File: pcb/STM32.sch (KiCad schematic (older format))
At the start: 43 parts

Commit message: stepper planes
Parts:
- removed RA1, RA2, RA3, RA4, RA5, RA6, RA7, RA8, RA9: 100k, Resistors_SMD:R_0603, symbol media_board:R-RESCUE-stamp_mini_4_layers
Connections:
- wire segments 209 -> 182
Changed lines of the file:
@@
 IO32
-$Comp
-L media_board:R-RESCUE-stamp_mini_4_layers RA1
-U 1 1 55660488
-P 850 2800
-F 0 "RA1" V 930 2800 50  0000 C CNN
-F 1 "100k" V 850 2800 50  0000 C CNN
-F 2 "Resistors_SMD:R_0603" H 850 2800 60  0001 C CNN
-F 3 "" H 850 2800 60  0001 C CNN
-	1    850  2800
-	-1   0    0    1
-$EndComp
-$Comp
-L media_board:R-RESCUE-stamp_mini_4_layers RA2
-U 1 1 55660A61
-P 1000 2800
-F 0 "RA2" V 1080 2800 50  0000 C CNN
-F 1 "100k" V 1000 2800 50  0000 C CNN
-F 2 "Resistors_SMD:R_0603" H 1000 2800 60  0001 C CNN
-F 3 "" H 1000 2800 60  0001 C CNN
-	1    1000 2800
-	-1   0    0    1
-$EndComp
-$Comp
-L media_board:R-RESCUE-stamp_mini_4_layers RA3
-U 1 1 55660AB1
-P 1150 2800
-F 0 "RA3" V 1230 2800 50  0000 C CNN
-F 1 "100k" V 1150 2800 50  0000 C CNN
-F 2 "Resistors_SMD:R_0603" H 1150 2800 60  0001 C CNN
-F 3 "" H 1150 2800 60  0001 C CNN
-	1    1150 2800
-	-1   0    0    1
-$EndComp
-$Comp
-L media_board:R-RESCUE-stamp_mini_4_layers RA4
-U 1 1 55660AFE
-P 1300 2800
-F 0 "RA4" V 1380 2800 50  0000 C CNN
-F 1 "100k" V 1300 2800 50  0000 C CNN
-F 2 "Resistors_SMD:R_0603" H 1300 2800 60  0001 C CNN
-F 3 "" H 1300 2800 60  0001 C CNN
-	1    1300 2800
-	-1   0    0    1
-$EndComp
-$Comp
-L media_board:R-RESCUE-stamp_mini_4_layers RA5
-U 1 1 55660B50
-P 1450 2800
-F 0 "RA5" V 1530 2800 50  0000 C CNN
-F 1 "100k" V 1450 2800 50  0000 C CNN
-F 2 "Resistors_SMD:R_0603" H 1450 2800 60  0001 C CNN
-F 3 "" H 1450 2800 60  0001 C CNN
-	1    1450 2800
-	-1   0    0    1
-$EndComp
-$Comp
-L media_board:R-RESCUE-stamp_mini_4_layers RA6
-U 1 1 55660BA7
-P 1600 2800
-F 0 "RA6" V 1680 2800 50  0000 C CNN
-F 1 "100k" V 1600 2800 50  0000 C CNN
-F 2 "Resistors_SMD:R_0603" H 1600 2800 60  0001 C CNN
-F 3 "" H 1600 2800 60  0001 C CNN
-	1    1600 2800
-	-1   0    0    1
-$EndComp
-$Comp
-L media_board:R-RESCUE-stamp_mini_4_layers RA7
-U 1 1 55660C05
-P 1750 2800
-F 0 "RA7" V 1830 2800 50  0000 C CNN
-F 1 "100k" V 1750 2800 50  0000 C CNN
-F 2 "Resistors_SMD:R_0603" H 1750 2800 60  0001 C CNN
-F 3 "" H 1750 2800 60  0001 C CNN
-	1    1750 2800
-	-1   0    0    1
-$EndComp
-$Comp
-L media_board:R-RESCUE-stamp_mini_4_layers RA8
-U 1 1 55660C68
-P 1900 2800
-F 0 "RA8" V 1980 2800 50  0000 C CNN
-F 1 "100k" V 1900 2800 50  0000 C CNN
-F 2 "Resistors_SMD:R_0603" H 1900 2800 60  0001 C CNN
-F 3 "" H 1900 2800 60  0001 C CNN
-	1    1900 2800
-	-1   0    0    1
-$EndComp
-$Comp
-L media_board:GND-RESCUE-stamp_mini_4_layers #PWR0168
-U 1 1 556636B2
-P 850 3150
-F 0 "#PWR0168" H 850 3150 30  0001 C CNN
-F 1 "GND" H 850 3080 30  0001 C CNN
-F 2 "" H 850 3150 60  0001 C CNN
-F 3 "" H 850 3150 60  0001 C CNN
-	1    850  3150
-	1    0    0    -1
-$EndComp
 $Comp
 L media_board:JUMPER PGM1
@@
 	5050 6650 5050 6750
 Wire Wire Line
-	750  1800 1900 1800
-Wire Wire Line
 	2250 3900 2600 3900
 Wire Wire Line
@@
 	2600 3300 2250 3300
 Wire Wire Line
-	750  2500 850  2500
-Wire Wire Line
-	750  2300 1150 2300
-Wire Wire Line
-	750  2100 1450 2100
-Wire Wire Line
-	750  1900 1750 1900
-Wire Wire Line
 	4250 6550 4250 6650
 Wire Wire Line
@@
 	2300 1400 2600 1400
 Wire Wire Line
-	750  2000 1600 2000
-Wire Wire Line
 	4500 800  4500 950
 Wire Wire Line
@@
 Wire Wire Line
 	2250 3800 2600 3800
-Wire Wire Line
-	750  2200 1300 2200
-Wire Wire Line
-	750  2400 1000 2400
 Wire Wire Line
 	4250 6650 4450 6650
@@
 Wire Wire Line
 	6000 4200 5600 4200
-Wire Wire Line
-	850  2550 850  2500
-Connection ~ 850  2500
-Wire Wire Line
-	1000 2550 1000 2400
-Connection ~ 1000 2400
-Wire Wire Line
-	1150 2550 1150 2300
-Connection ~ 1150 2300
-Wire Wire Line
-	1300 2550 1300 2200
-Connection ~ 1300 2200
-Wire Wire Line
-	1450 2550 1450 2100
-Connection ~ 1450 2100
-Wire Wire Line
-	1600 2550 1600 2000
-Connection ~ 1600 2000
-Wire Wire Line
-	1750 2550 1750 1900
-Connection ~ 1750 1900
-Wire Wire Line
-	1900 2550 1900 1800
-Connection ~ 1900 1800
-Wire Wire Line
-	850  3050 850  3150
 Wire Wire Line
 	7400 7900 7550 7900
@@
 Wire Wire Line
 	6900 3550 7200 3550
-Wire Wire Line
-	850  2500 2600 2500
-Wire Wire Line
-	1000 2400 2600 2400
-Wire Wire Line
-	1150 2300 2600 2300
-Wire Wire Line
-	1300 2200 2600 2200
-Wire Wire Line
-	1450 2100 2600 2100
-Wire Wire Line
-	1600 2000 2600 2000
-Wire Wire Line
-	1750 1900 2600 1900
-Wire Wire Line
-	1900 1800 2600 1800
 Wire Wire Line
 	5600 1950 6900 1950
@@
 Text Label 800  3500 0    50   ~ 0
 SEN8
-Wire Wire Line
-	750  3500 850  3500
-Wire Wire Line
-	850  3550 850  3500
-Connection ~ 850  3500
-Wire Wire Line
-	850  3500 2600 3500
-$Comp
-L media_board:R-RESCUE-stamp_mini_4_layers RA9
-U 1 1 5EA6155C
-P 850 3800
-F 0 "RA9" V 930 3800 50  0000 C CNN
-F 1 "100k" V 850 3800 50  0000 C CNN
-F 2 "Resistors_SMD:R_0603" H 850 3800 60  0001 C CNN
-F 3 "" H 850 3800 60  0001 C CNN
-	1    850  3800
-	-1   0    0    1
-$EndComp
-$Comp
-L media_board:GND-RESCUE-stamp_mini_4_layers #PWR0220
-U 1 1 5EA6E32C
-P 850 4150
-F 0 "#PWR0220" H 850 4150 30  0001 C CNN
-F 1 "GND" H 850 4080 30  0001 C CNN
-F 2 "" H 850 4150 60  0001 C CNN
-F 3 "" H 850 4150 60  0001 C CNN
-	1    850  4150
-	1    0    0    -1
-$EndComp
-Wire Wire Line
-	850  4050 850  4150
 Text Label 800  2500 0    50   ~ 0
 SEN7
@@
 Text HLabel 9050 1300 2    50   Input ~ 0
 SEN[0..8]
-Wire Wire Line
-	1900 3050 1750 3050
-Connection ~ 850  3050
-Connection ~ 1000 3050
-Wire Wire Line
-	1000 3050 850  3050
-Connection ~ 1150 3050
-Wire Wire Line
-	1150 3050 1000 3050
-Connection ~ 1300 3050
-Wire Wire Line
-	1300 3050 1150 3050
-Connection ~ 1450 3050
-Wire Wire Line
-	1450 3050 1300 3050
-Connection ~ 1600 3050
-Wire Wire Line
-	1600 3050 1450 3050
-Wire Wire Line
-	1600 3050 1750 3050
 Wire Bus Line
 	5950 2850 5950 3550
 Wire Bus Line
 	8950 1300 8950 2100
-Connection ~ 1750 3050
+Wire Wire Line
+	750  3500 2600 3500
+Wire Wire Line
+	750  1800 2600 1800
+Wire Wire Line
+	750  1900 2600 1900
+Wire Wire Line
+	750  2000 2600 2000
+Wire Wire Line
+	750  2100 2600 2100
+Wire Wire Line
+	750  2200 2600 2200
+Wire Wire Line
+	750  2300 2600 2300
+Wire Wire Line
+	750  2400 2600 2400
+Wire Wire Line
+	750  2500 2600 2500
 $EndSCHEMATC

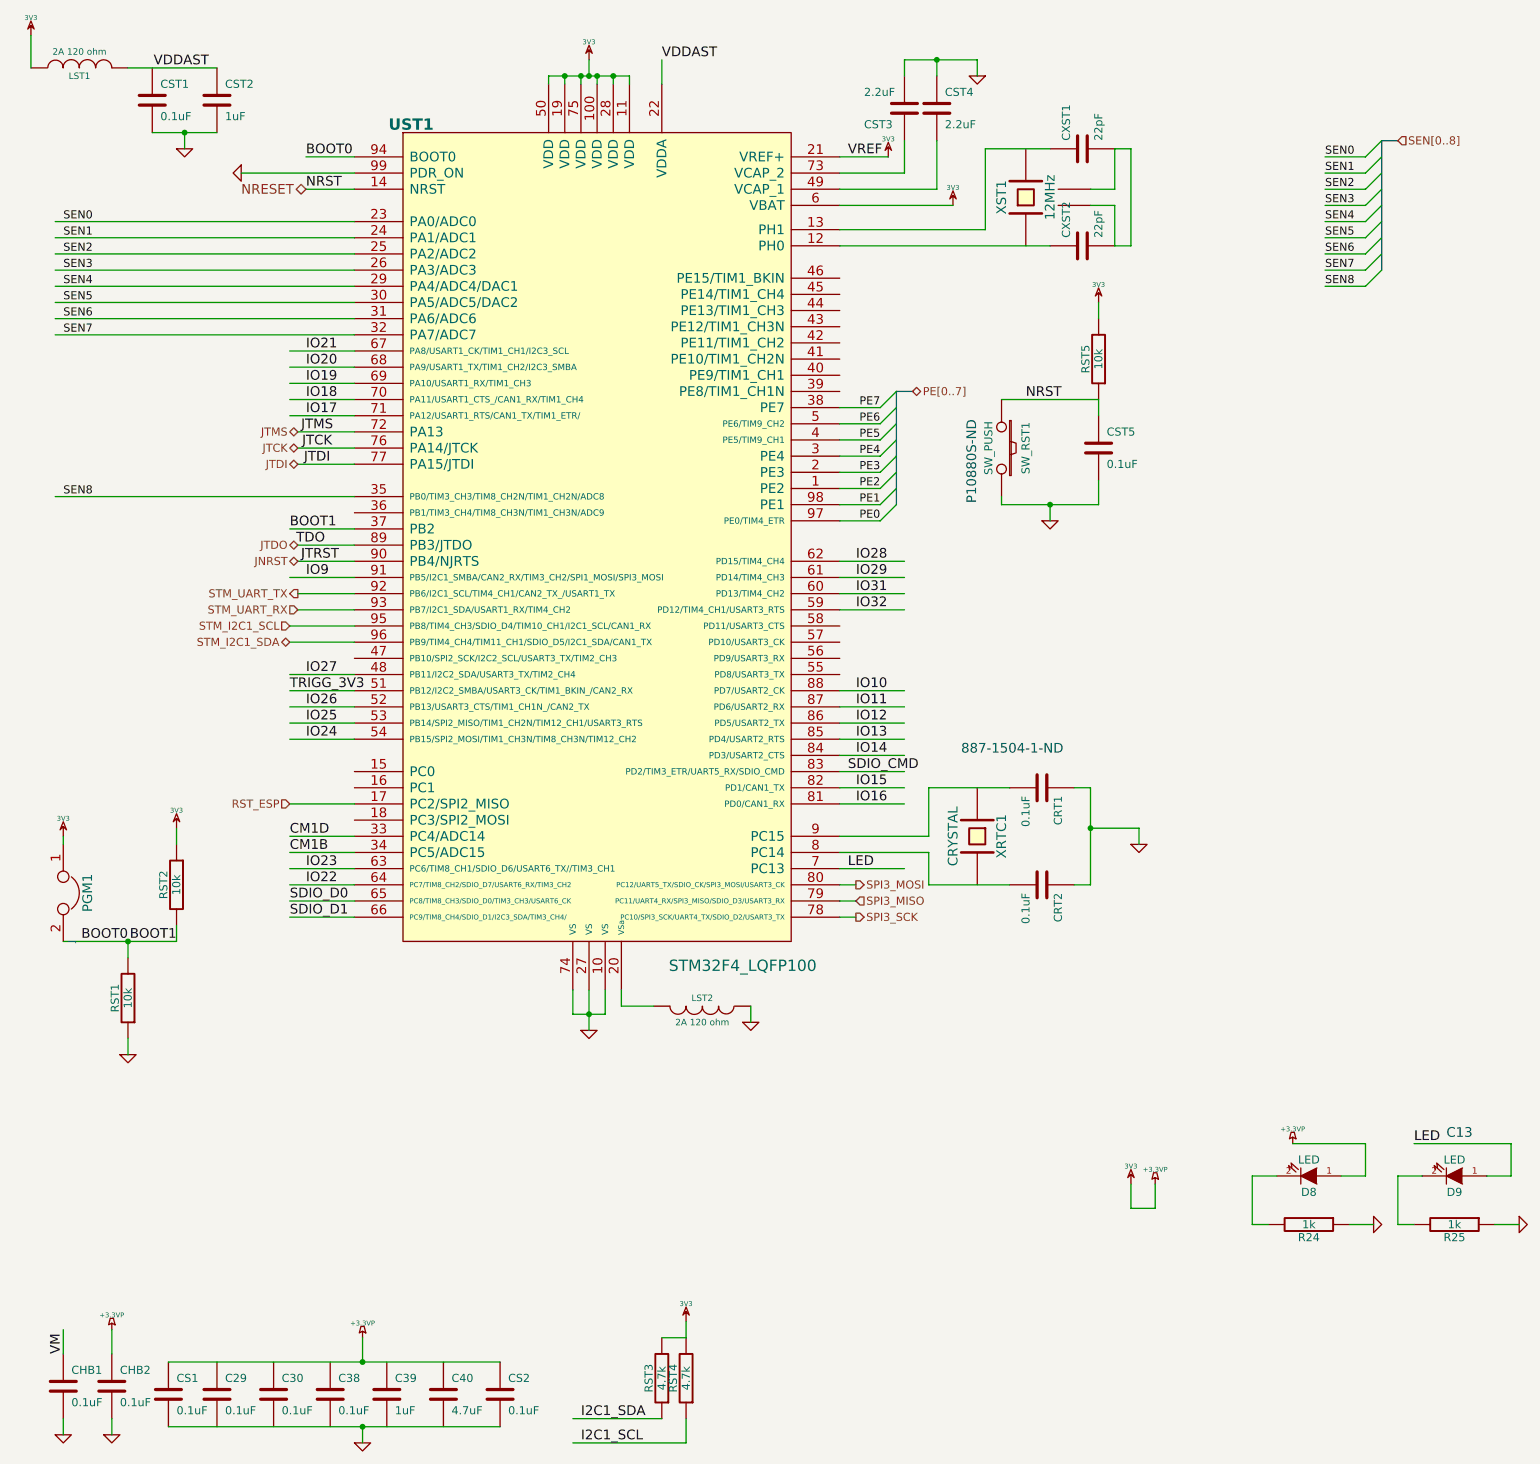
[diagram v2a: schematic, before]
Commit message: Added 3V3_STM in STM32F4 and supply sheets
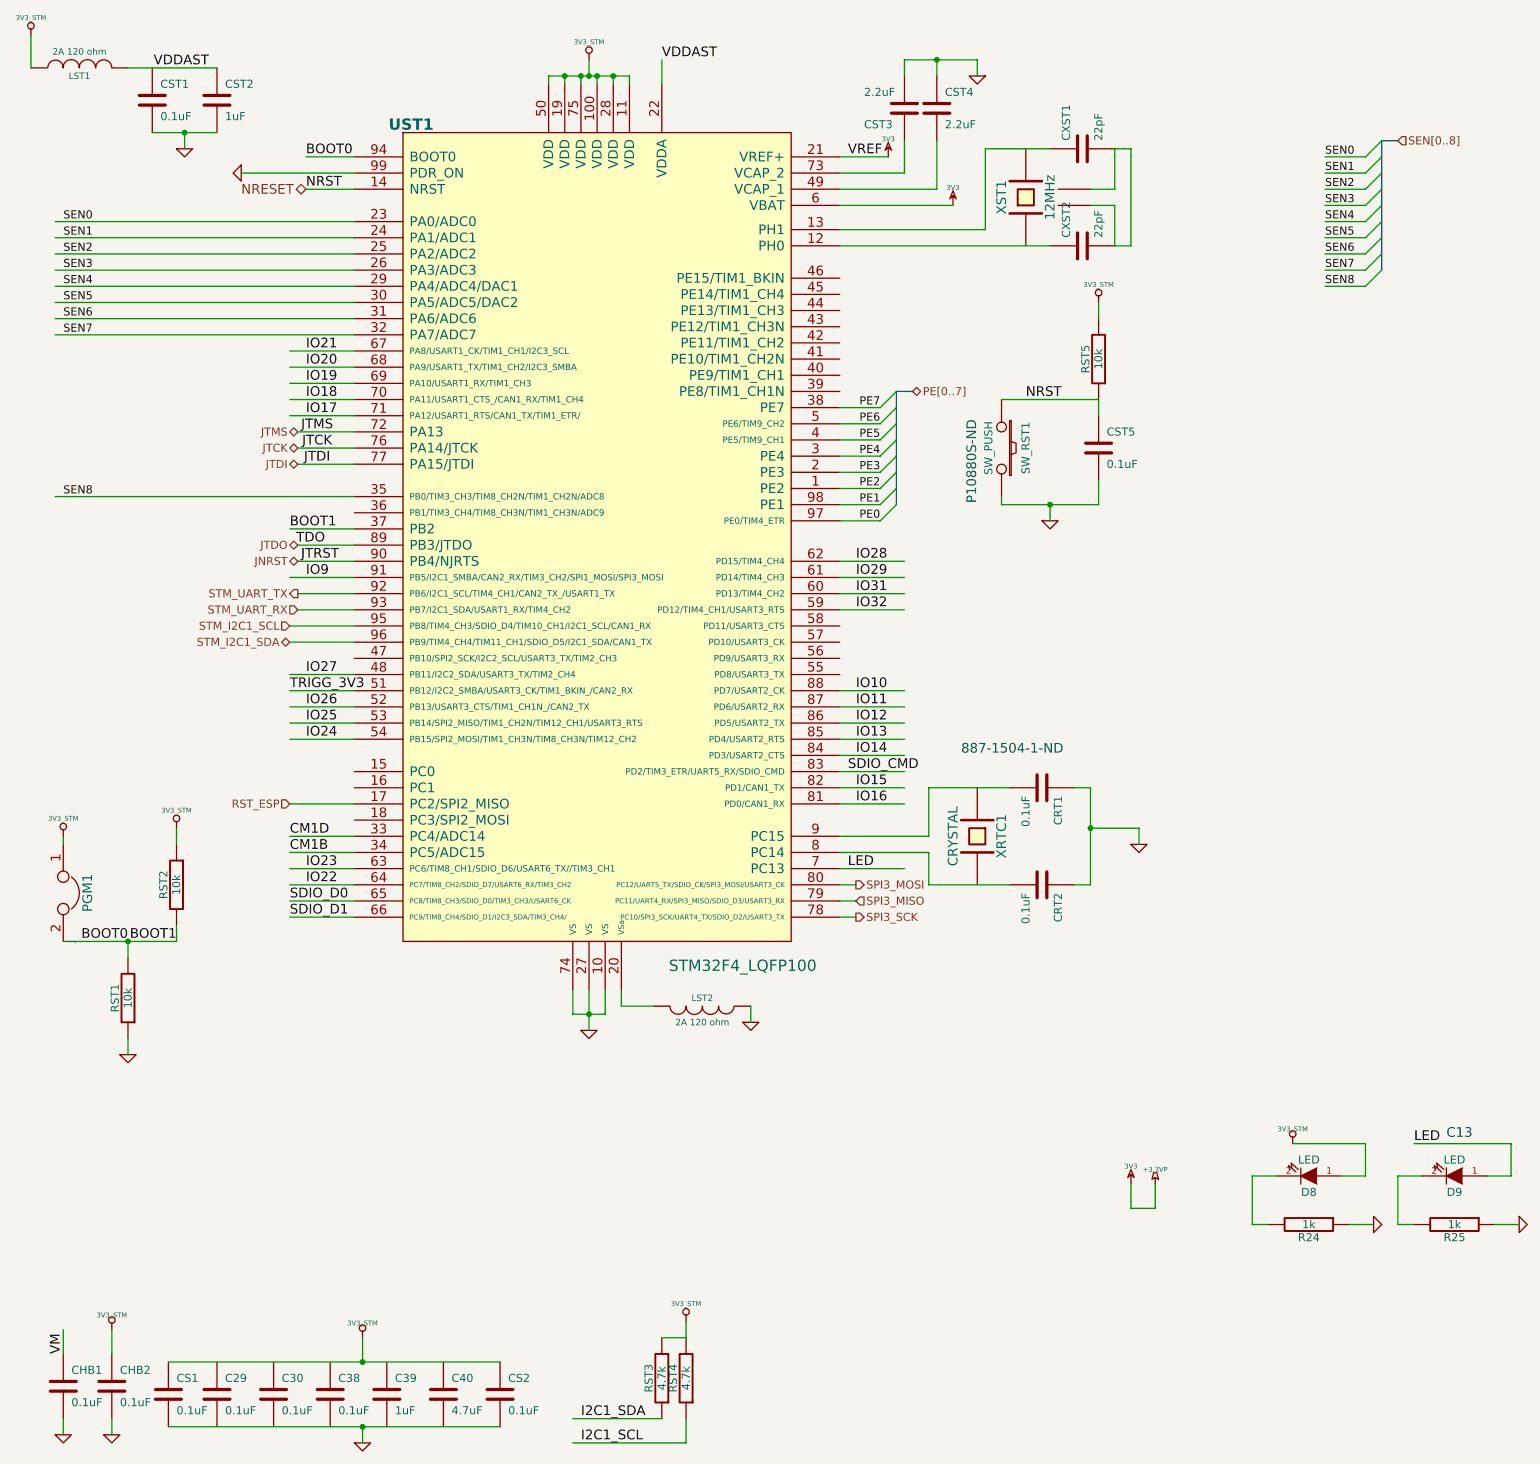
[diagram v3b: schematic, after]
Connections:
- net labels added: 3V3_STM
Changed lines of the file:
@@
 $EndComp
 $Comp
-L media_board:+3.3VP #PWR0122
+L ventilator-PowerSymbols:3V3_STM #PWR0122
 U 1 1 516D629C
 P 8400 7500
 F 0 "#PWR0122" H 8450 7530 20  0001 C CNN
-F 1 "+3.3VP" H 8400 7590 30  0000 C CNN
+F 1 "3V3_STM" H 8400 7590 30  0000 C CNN
 F 2 "" H 8400 7500 60  0001 C CNN
 F 3 "" H 8400 7500 60  0001 C CNN
@@
 $EndComp
 $Comp
-L media_board:+3.3VP #PWR0123
+L ventilator-PowerSymbols:3V3_STM #PWR0123
 U 1 1 516D625C
 P 2650 8700
 F 0 "#PWR0123" H 2700 8730 20  0001 C CNN
-F 1 "+3.3VP" H 2650 8790 30  0000 C CNN
+F 1 "3V3_STM" H 2650 8790 30  0000 C CNN
 F 2 "" H 2650 8700 60  0001 C CNN
 F 3 "" H 2650 8700 60  0001 C CNN
@@
 $EndComp
 $Comp
-L media_board:+3.3VP #PWR0128
+L ventilator-PowerSymbols:3V3_STM #PWR0128
 U 1 1 5344E9B7
 P 1100 8650
 F 0 "#PWR0128" H 1150 8680 20  0001 C CNN
-F 1 "+3.3VP" H 1100 8740 30  0000 C CNN
+F 1 "3V3_STM" H 1100 8740 30  0000 C CNN
 F 2 "" H 1100 8650 60  0001 C CNN
 F 3 "" H 1100 8650 60  0001 C CNN
@@
 JTDI
 $Comp
-L media_board:3V3 #PWR0148
+L ventilator-PowerSymbols:3V3_STM #PWR0148
 U 1 1 545549BD
 P 4050 800
 F 0 "#PWR0148" H 4050 900 30  0001 C CNN
-F 1 "3V3" H 4050 910 30  0000 C CNN
+F 1 "3V3_STM" H 4050 910 30  0000 C CNN
 F 2 "" H 4050 800 60  0001 C CNN
 F 3 "" H 4050 800 60  0001 C CNN
@@
 $EndComp
 $Comp
-L media_board:3V3 #PWR0149
+L ventilator-PowerSymbols:3V3_STM #PWR0149
 U 1 1 54556556
 P 600 650
 F 0 "#PWR0149" H 600 750 30  0001 C CNN
-F 1 "3V3" H 600 760 30  0000 C CNN
+F 1 "3V3_STM" H 600 760 30  0000 C CNN
 F 2 "" H 600 650 60  0001 C CNN
 F 3 "" H 600 650 60  0001 C CNN
@@
 $EndComp
 $Comp
-L media_board:3V3 #PWR0151
+L ventilator-PowerSymbols:3V3_STM #PWR0151
 U 1 1 54557AB0
 P 4650 8600
 F 0 "#PWR0151" H 4650 8700 30  0001 C CNN
-F 1 "3V3" H 4650 8710 30  0000 C CNN
+F 1 "3V3_STM" H 4650 8710 30  0000 C CNN
 F 2 "" H 4650 8600 60  0001 C CNN
 F 3 "" H 4650 8600 60  0001 C CNN
@@
 $EndComp
 $Comp
-L media_board:3V3 #PWR0158
+L ventilator-PowerSymbols:3V3_STM #PWR0158
 U 1 1 545655B0
 P 7200 2300
 F 0 "#PWR0158" H 7200 2400 30  0001 C CNN
-F 1 "3V3" H 7200 2410 30  0000 C CNN
+F 1 "3V3_STM" H 7200 2410 30  0000 C CNN
 F 2 "" H 7200 2300 60  0001 C CNN
 F 3 "" H 7200 2300 60  0001 C CNN
@@
 $EndComp
 $Comp
-L media_board:3V3 #PWR0166
+L ventilator-PowerSymbols:3V3_STM #PWR0166
 U 1 1 5456BBE6
 P 1500 5550
 F 0 "#PWR0166" H 1500 5650 30  0001 C CNN
-F 1 "3V3" H 1500 5660 30  0000 C CNN
+F 1 "3V3_STM" H 1500 5660 30  0000 C CNN
 F 2 "" H 1500 5550 60  0001 C CNN
 F 3 "" H 1500 5550 60  0001 C CNN
@@
 $EndComp
 $Comp
-L media_board:3V3 #PWR0171
+L ventilator-PowerSymbols:3V3_STM #PWR0171
 U 1 1 5679F680
 P 800 5600
 F 0 "#PWR0171" H 800 5700 30  0001 C CNN
-F 1 "3V3" H 800 5710 30  0000 C CNN
+F 1 "3V3_STM" H 800 5710 30  0000 C CNN
 F 2 "" H 800 5600 60  0001 C CNN
 F 3 "" H 800 5600 60  0001 C CNN

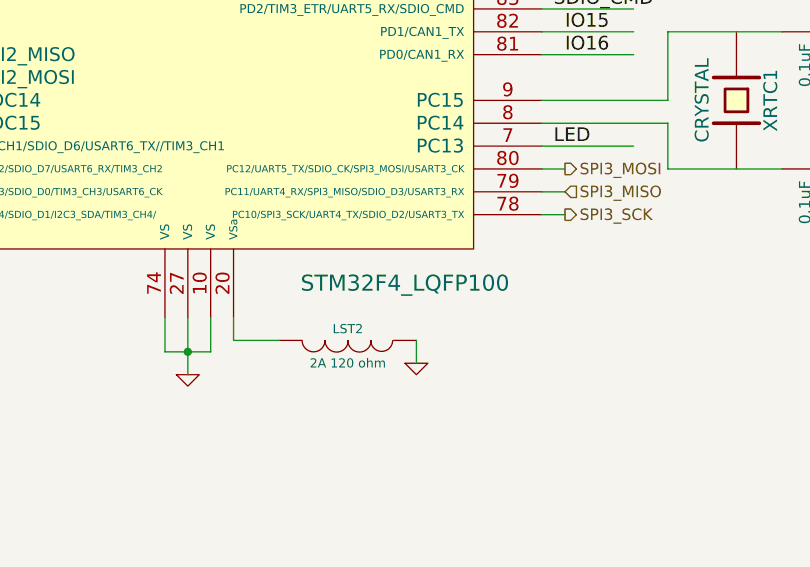
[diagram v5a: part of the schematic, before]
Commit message: routing analog signals
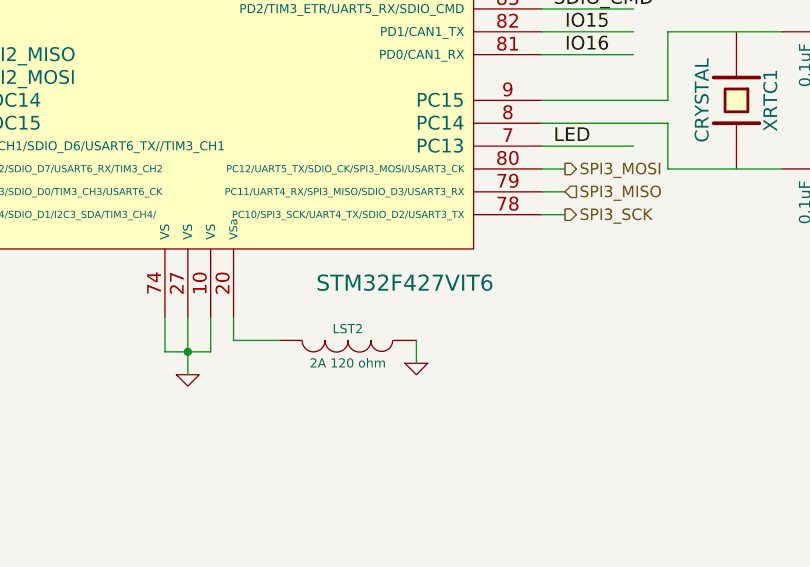
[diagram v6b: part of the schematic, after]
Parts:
- UST1: value STM32F4_LQFP100 -> STM32F427VIT6; DigiKey (none) -> 497-14049-ND
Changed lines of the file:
@@
 P 4200 3600
 F 0 "UST1" H 2950 6000 70  0000 C CNB
-F 1 "STM32F4_LQFP100" H 5000 800 70  0000 C CNN
+F 1 " STM32F427VIT6 " H 5000 800 70  0000 C CNN
 F 2 "Package_QFP:LQFP-100_14x14mm_P0.5mm" H 4200 3600 60  0001 C CNN
 F 3 "" H 4200 3600 60  0001 C CNN
+F 4 " 497-14049-ND " H 4200 3600 50  0001 C CNN "DigiKey"
 	1    4200 3600
 	1    0    0    -1
